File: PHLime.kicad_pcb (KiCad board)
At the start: 2 copper layers, 97 x 81.8 mm, 43 parts, among them J10 2P BT 2, J11 2P BT 3, J12 2P BT 4, J13 2P BT 5, J14 2P BT 6, J15 2P BT 7, J16 1P START, J17 EFFECT, J18 VEFX, J19 2P START, J2 1P BT 1, J20 P1 TT analog, J21 P2 TT analog, J22 LED P1 TT, J23 LED P2 TT, J24 LED P1 Console, J25 LED P2 Console, J26 LED CENTER, J27 USB Type C Connector, J28 P1 TT Encoder, J29 P2 TT Encoder, J3 1P BT 3, J4 1P BT 5, J5 1P BT 7, J6 1P BT 2, J7 1P BT 4, J8 1P BT 6, J9 2P BT 1, SW1 SW_Push, U1 AT90USB647-A, Y1 16MHz

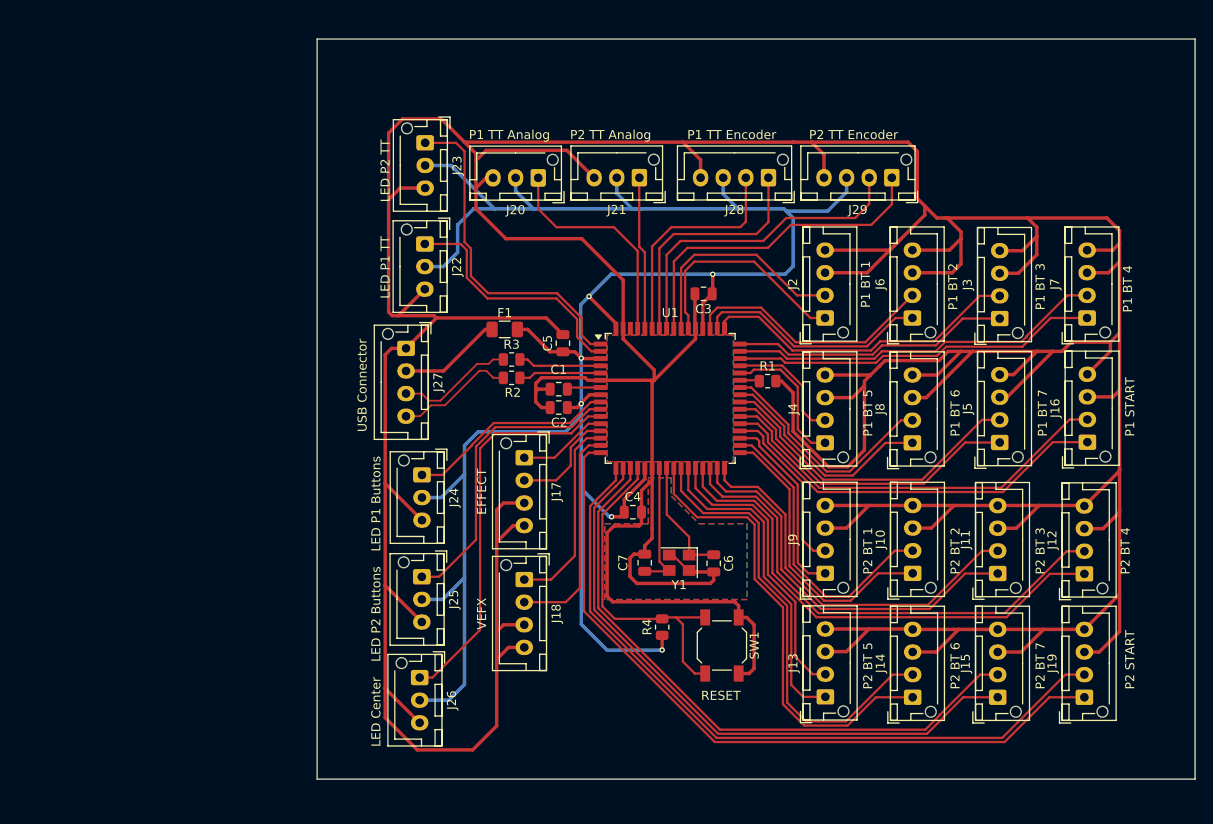
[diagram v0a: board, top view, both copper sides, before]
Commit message: Ground Planes OP
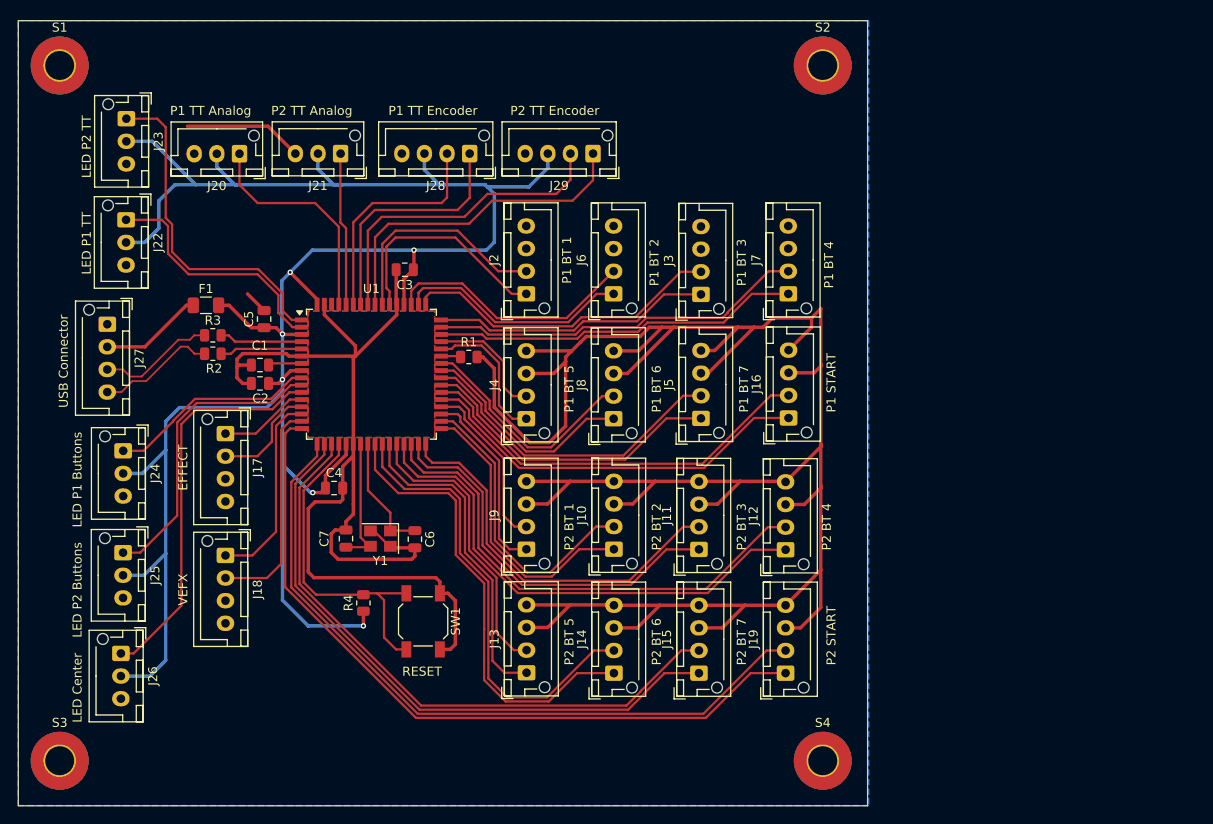
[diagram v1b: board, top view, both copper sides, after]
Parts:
- added S1: MountingHole_3.2mm_M3_Pad_TopBottom, Mounting Holes:MountingHole_3.2mm_M3_Pad_TopBottom, F.Cu at (22.4, 22.7)
- added S2: MountingHole_3.2mm_M3_Pad_TopBottom, Mounting Holes:MountingHole_3.2mm_M3_Pad_TopBottom, F.Cu at (106.7, 22.7)
- added S3: MountingHole_3.2mm_M3_Pad_TopBottom, Mounting Holes:MountingHole_3.2mm_M3_Pad_TopBottom, F.Cu at (22.4, 99.6)
- added S4: MountingHole_3.2mm_M3_Pad_TopBottom, Mounting Holes:MountingHole_3.2mm_M3_Pad_TopBottom, F.Cu at (106.7, 99.6)
- moved J11 33.1 mm to (93.0, 76.2)
- moved J12 33.1 mm to (102.6, 76.3)
- moved J15 33.1 mm to (93.0, 89.9)
- moved J19 33.1 mm to (102.6, 89.9)
- moved R1 33.1 mm to (67.6, 55.0)
- moved C3 33.1 mm to (60.5, 45.3)
- moved C7 33.1 mm to (54.0, 75.0)
- moved F1 33.1 mm to (38.5, 49.2)
- moved J20 33.1 mm to (42.2, 32.5)
- moved J21 33.1 mm to (53.4, 32.5)
- moved J22 33.1 mm to (29.7, 39.8)
- moved J24 33.1 mm to (29.4, 65.3)
- moved R2 33.1 mm to (39.3, 54.6)
- moved R3 33.1 mm to (39.3, 52.6)
- moved R4 33.1 mm to (55.9, 82.1)
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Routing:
- net GND: track 756.9 -> 384.0 mm
- removed copper zone on F.Cu, net GND
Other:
- board size 97 x 81.8 mm -> 93.9 x 86.8 mm

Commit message: Wow I feel really dumb for not doing this.
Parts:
- moved C5 6.85 mm to (50.3, 46.5), turned to 0 degrees
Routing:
- net GND: track 384.0 -> 126.1 mm, vias 0 -> 1
- added copper zone on F.Cu, net GND
